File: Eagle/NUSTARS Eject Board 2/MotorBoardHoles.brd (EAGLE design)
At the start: 44.4 x 40.3 mm, 13 parts, among them Q1 200mA/40V

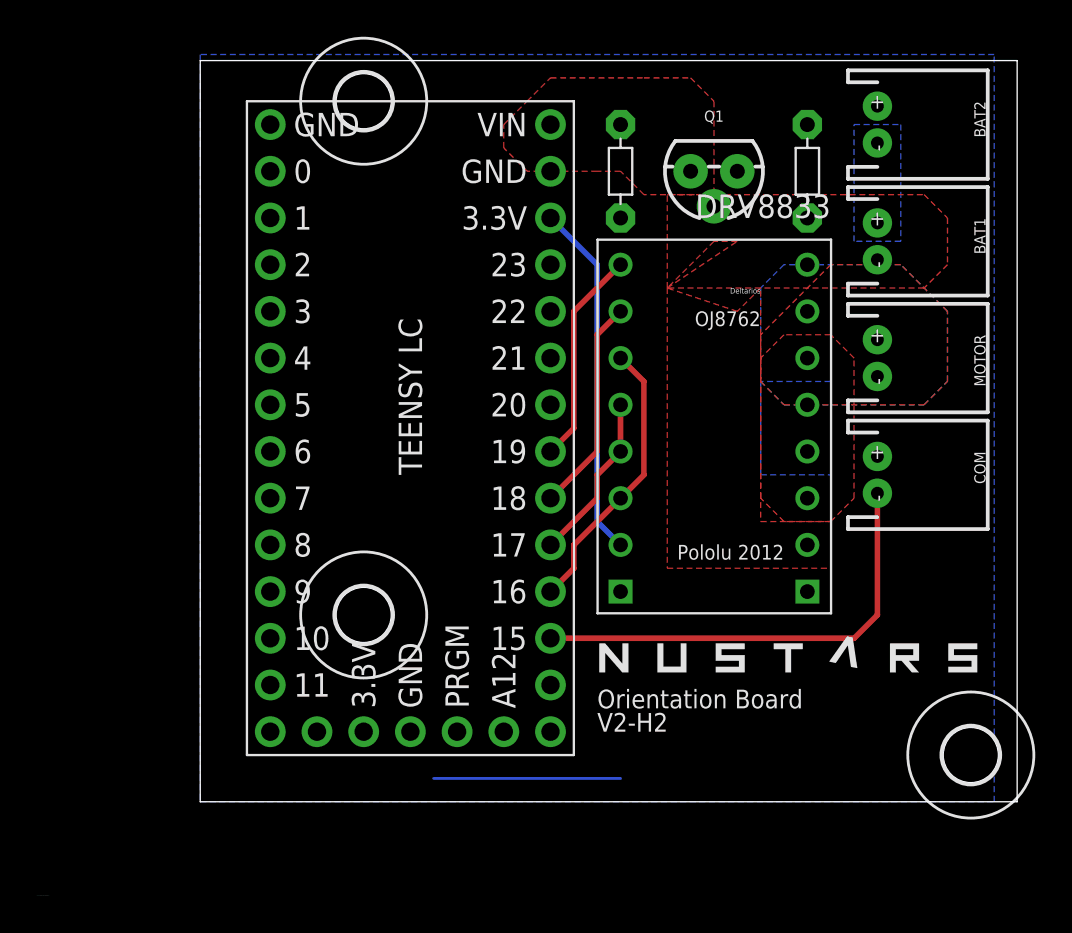
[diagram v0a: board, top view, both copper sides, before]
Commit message: Add rover
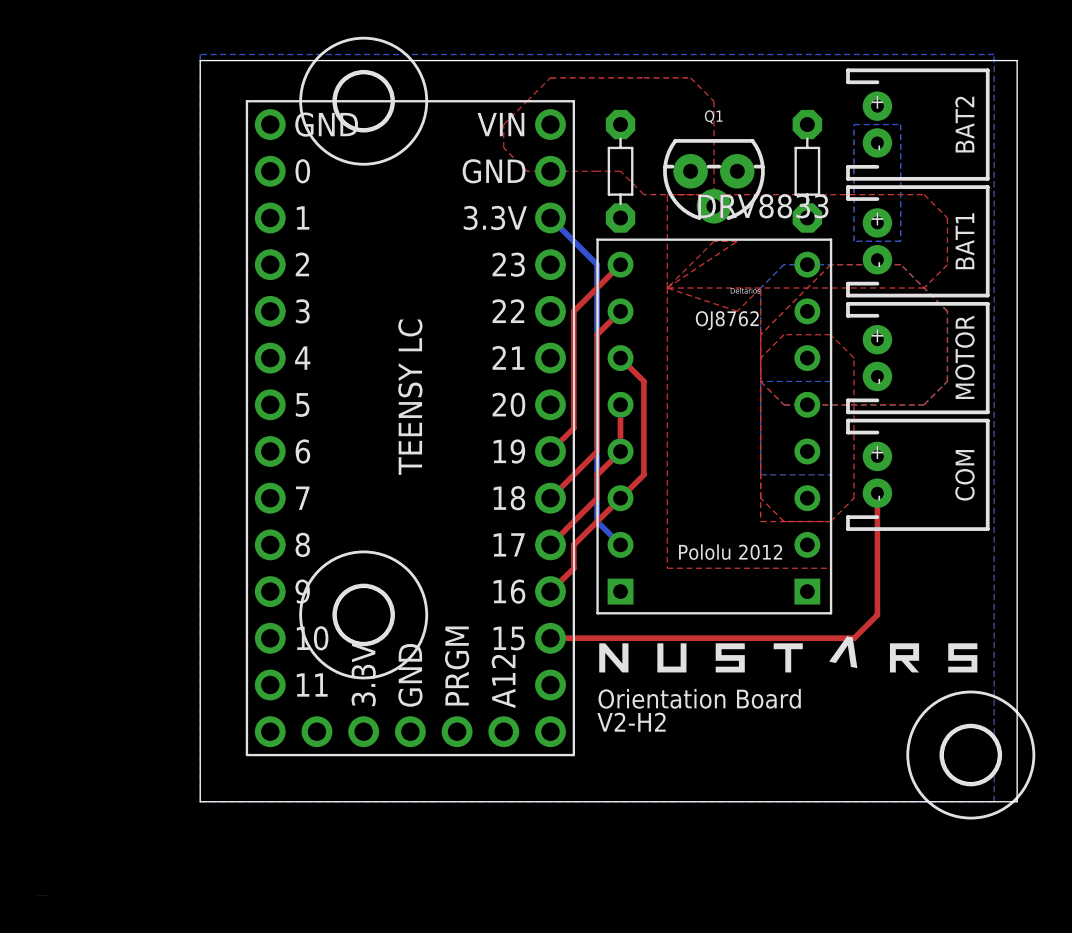
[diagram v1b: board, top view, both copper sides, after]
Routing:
- net GND: track 10.2 -> 0.00 mm
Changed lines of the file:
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@@
 </class>
 </classes>
-<designrules name="default">
-<description language="de">&lt;b&gt;EAGLE Design Rules&lt;/b&gt;
-&lt;p&gt;
-Die Standard-Design-Rules sind so gewählt, dass sie für
-die meisten Anwendungen passen. Sollte ihre Platine
-besondere Anforderungen haben, treffen Sie die erforderlichen
-Einstellungen hier und speichern die Design Rules unter
-einem neuen Namen ab.</description>
+<designrules name="SparkFun">
 <description language="en">&lt;b&gt;EAGLE Design Rules&lt;/b&gt;
 &lt;p&gt;
@@
 <param name="mtCopper" value="0.035mm 0.035mm 0.035mm 0.035mm 0.035mm 0.035mm 0.035mm 0.035mm 0.035mm 0.035mm 0.035mm 0.035mm 0.035mm 0.035mm 0.035mm 0.035mm"/>
 <param name="mtIsolate" value="1.5mm 0.15mm 0.2mm 0.15mm 0.2mm 0.15mm 0.2mm 0.15mm 0.2mm 0.15mm 0.2mm 0.15mm 0.2mm 0.15mm 0.2mm"/>
-<param name="mdWireWire" value="6mil"/>
-<param name="mdWirePad" value="6mil"/>
-<param name="mdWireVia" value="6mil"/>
-<param name="mdPadPad" value="6mil"/>
-<param name="mdPadVia" value="6mil"/>
-<param name="mdViaVia" value="6mil"/>
-<param name="mdSmdPad" value="6mil"/>
-<param name="mdSmdVia" value="6mil"/>
-<param name="mdSmdSmd" value="6mil"/>
-<param name="mdViaViaSameLayer" value="6mil"/>
+<param name="mdWireWire" value="8mil"/>
+<param name="mdWirePad" value="8mil"/>
+<param name="mdWireVia" value="8mil"/>
+<param name="mdPadPad" value="8mil"/>
+<param name="mdPadVia" value="8mil"/>
+<param name="mdViaVia" value="8mil"/>
+<param name="mdSmdPad" value="8mil"/>
+<param name="mdSmdVia" value="8mil"/>
+<param name="mdSmdSmd" value="8mil"/>
+<param name="mdViaViaSameLayer" value="8mil"/>
 <param name="mnLayersViaInSmd" value="2"/>
-<param name="mdCopperDimension" value="40mil"/>
-<param name="mdDrill" value="6mil"/>
+<param name="mdCopperDimension" value="10mil"/>
+<param name="mdDrill" value="8mil"/>
 <param name="mdSmdStop" value="0mil"/>
-<param name="msWidth" value="6mil"/>
-<param name="msDrill" value="0.35mm"/>
+<param name="msWidth" value="8mil"/>
+<param name="msDrill" value="20mil"/>
 <param name="msMicroVia" value="9.99mm"/>
 <param name="msBlindViaRatio" value="0.5"/>
@@
 <param name="rvMicroViaOuter" value="0.25"/>
 <param name="rvMicroViaInner" value="0.25"/>
-<param name="rlMinPadTop" value="10mil"/>
+<param name="rlMinPadTop" value="12mil"/>
 <param name="rlMaxPadTop" value="20mil"/>
 <param name="rlMinPadInner" value="10mil"/>
 <param name="rlMaxPadInner" value="20mil"/>
-<param name="rlMinPadBottom" value="10mil"/>
+<param name="rlMinPadBottom" value="12mil"/>
 <param name="rlMaxPadBottom" value="20mil"/>
-<param name="rlMinViaOuter" value="8mil"/>
+<param name="rlMinViaOuter" value="10mil"/>
 <param name="rlMaxViaOuter" value="20mil"/>
-<param name="rlMinViaInner" value="8mil"/>
+<param name="rlMinViaInner" value="10mil"/>
 <param name="rlMaxViaInner" value="20mil"/>
 <param name="rlMinMicroViaOuter" value="4mil"/>
@@
 <param name="mlMinCreamFrame" value="0mil"/>
 <param name="mlMaxCreamFrame" value="0mil"/>
-<param name="mlViaStopLimit" value="0mil"/>
+<param name="mlViaStopLimit" value="25mil"/>
 <param name="srRoundness" value="0"/>
 <param name="srMinRoundness" value="0mil"/>
@@
 <element name="U$1" library="IchiCustoms" package="TEENSYLC" value="TEENSYLC" x="11.43" y="43.18" smashed="yes" rot="R270"/>
 <element name="BAT1" library="SparkFun-Connectors" library_urn="urn:adsk.eagle:library:513" package="JST-2-PTH" package3d_urn="urn:adsk.eagle:package:38053/1" value="" x="45.72" y="35.56" smashed="yes" rot="R270">
-<attribute name="NAME" x="50.99" y="36.83" size="0.6096" layer="21" font="vector" ratio="20" rot="R270"/>
+<attribute name="NAME" x="50.99" y="35.56" size="1.016" layer="21" font="vector" ratio="20" rot="R270" align="top-center"/>
 <attribute name="PROD_ID" value="CONN-09863" x="45.72" y="35.56" size="1.778" layer="27" rot="R270" display="off"/>
 <attribute name="SKU" value="PRT-09914" x="45.72" y="35.56" size="1.778" layer="27" rot="R270" display="off"/>
@@
 </element>
 <element name="BAT2" library="SparkFun-Connectors" library_urn="urn:adsk.eagle:library:513" package="JST-2-PTH" package3d_urn="urn:adsk.eagle:package:38053/1" value="" x="45.72" y="41.91" smashed="yes" rot="R270">
-<attribute name="NAME" x="50.99" y="43.18" size="0.6096" layer="21" font="vector" ratio="20" rot="R270"/>
+<attribute name="NAME" x="50.99" y="41.91" size="1.016" layer="21" font="vector" ratio="20" rot="R270" align="top-center"/>
 <attribute name="PROD_ID" value="CONN-09863" x="45.72" y="41.91" size="1.778" layer="27" rot="R270" display="off"/>
 <attribute name="SKU" value="PRT-09914" x="45.72" y="41.91" size="1.778" layer="27" rot="R270" display="off"/>
@@
 </element>
 <element name="COM" library="SparkFun-Connectors" library_urn="urn:adsk.eagle:library:513" package="JST-2-PTH" package3d_urn="urn:adsk.eagle:package:38053/1" value="" x="45.72" y="22.86" smashed="yes" rot="R270">
-<attribute name="NAME" x="50.99" y="24.13" size="0.6096" layer="21" font="vector" ratio="20" rot="R270"/>
+<attribute name="NAME" x="50.99" y="22.86" size="1.016" layer="21" font="vector" ratio="20" rot="R270" align="top-center"/>
 <attribute name="PROD_ID" value="CONN-09863" x="45.72" y="22.86" size="1.778" layer="27" rot="R270" display="off"/>
 <attribute name="SKU" value="PRT-09914" x="45.72" y="22.86" size="1.778" layer="27" rot="R270" display="off"/>
@@
 </element>
 <element name="MOTOR" library="SparkFun-Connectors" library_urn="urn:adsk.eagle:library:513" package="JST-2-PTH" package3d_urn="urn:adsk.eagle:package:38053/1" value="" x="45.72" y="29.21" smashed="yes" rot="R270">
-<attribute name="NAME" x="50.99" y="30.48" size="0.6096" layer="21" font="vector" ratio="20" rot="R270"/>
+<attribute name="NAME" x="50.99" y="29.21" size="1.016" layer="21" font="vector" ratio="20" rot="R270" align="top-center"/>
 <attribute name="PROD_ID" value="CONN-09863" x="45.72" y="29.21" size="1.778" layer="27" rot="R270" display="off"/>
 <attribute name="SKU" value="PRT-09914" x="45.72" y="29.21" size="1.778" layer="27" rot="R270" display="off"/>
@@
 </signal>
 <signal name="GND">
-<wire x1="31.75" y1="6.35" x2="21.59" y2="6.35" width="0.1524" layer="16"/>
-<polygon width="0.1524" layer="16" isolate="0.3048" rank="6">
+<polygon width="0.3048" layer="16" isolate="0.3048" rank="6">
 <vertex x="8.89" y="45.72"/>
 <vertex x="8.89" y="5.08"/>
@@
 <vertex x="40.64" y="30.48"/>
 </polygon>
-<polygon width="0.1524" layer="1" isolate="0.3048" thermals="no" rank="3">
+<polygon width="0.3048" layer="1" isolate="0.3048" thermals="no" rank="3">
 <vertex x="43.18" y="34.29"/>
 <vertex x="39.37" y="30.48"/>
@@
 <vertex x="43.18" y="27.94"/>
 </polygon>
-<polygon width="0.1524" layer="16" isolate="0.3048" thermals="no">
+<polygon width="0.3048" layer="16" isolate="0.3048" thermals="no">
 <vertex x="40.64" y="34.29"/>
 <vertex x="39.37" y="33.02"/>
